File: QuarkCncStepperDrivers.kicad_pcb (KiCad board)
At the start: 4 copper layers, 35.6 x 41.9 mm, 61 parts, among them J1 Conn_01x14, J2 Conn_01x14, Q1 AO4264E, Q2 AO4264E, Q3 AO4264E, Q4 AO4264E, Q5 AO4264E, Q6 AO4264E, Q7 AO4264E, Q8 AO4264E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

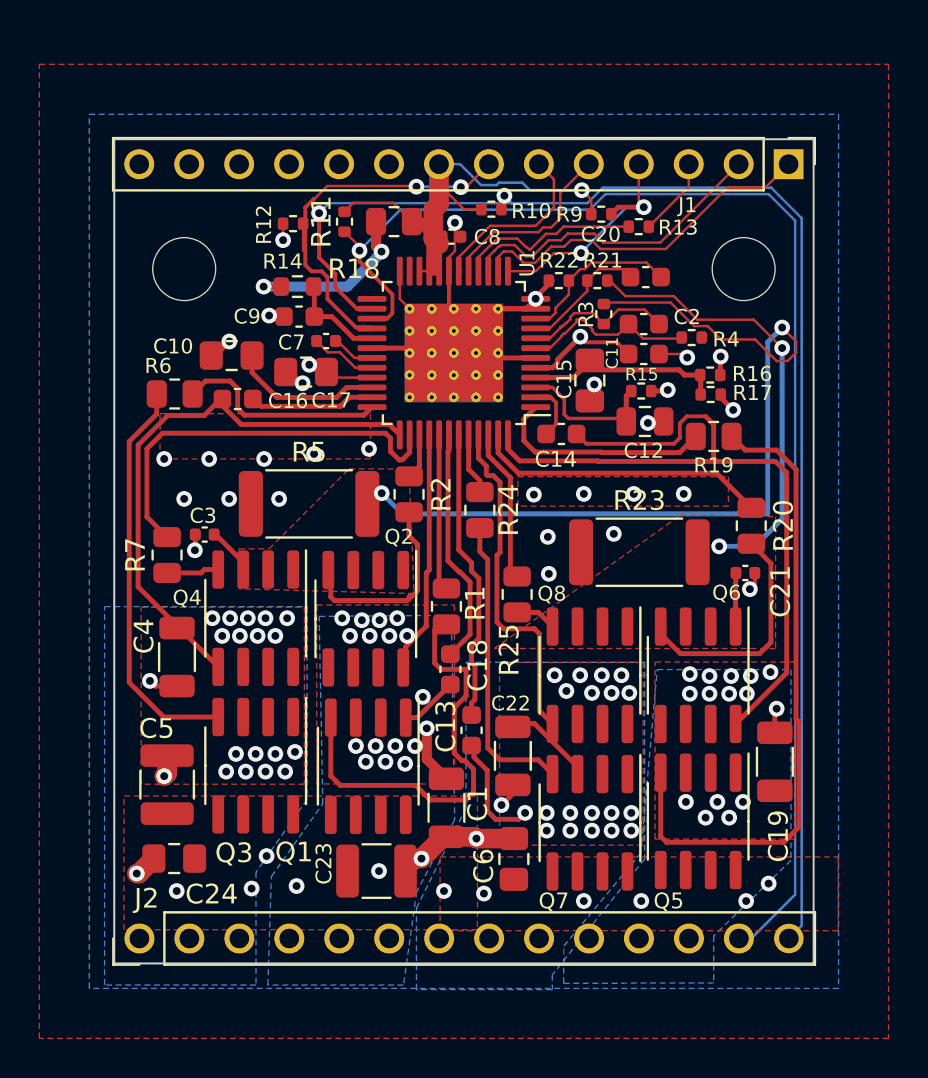
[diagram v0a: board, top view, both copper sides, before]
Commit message: Removed 0Ohms. Keyed design
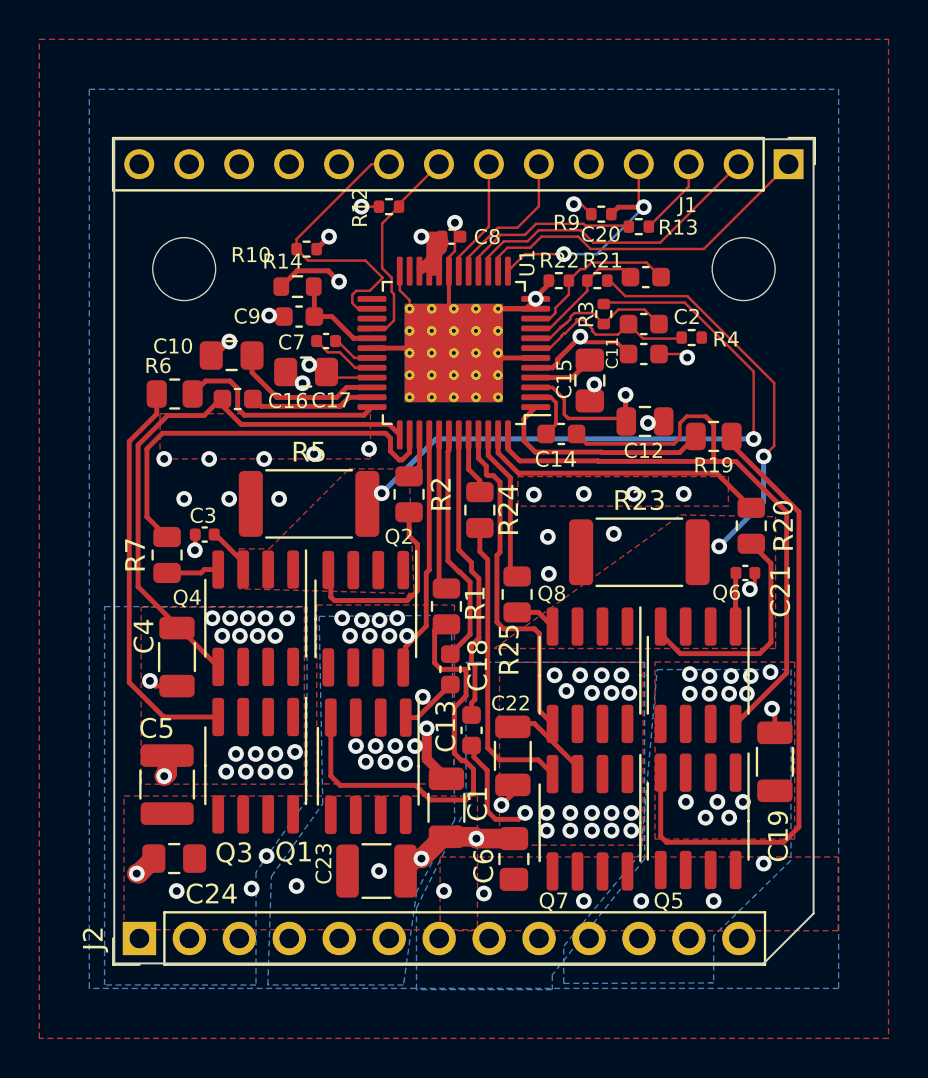
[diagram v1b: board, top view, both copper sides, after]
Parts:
- removed R11: 10k 1%, Resistor_SMD:R_0402_1005Metric
- removed R15: 0R, Resistor_SMD:R_0402_1005Metric
- removed R16, R17: 0R DNI, Resistor_SMD:R_0402_1005Metric
- removed R18: 0R DNI, Resistor_SMD:R_0805_2012Metric
- J2: value Conn_01x14 -> Conn_01x13; footprint Connector_PinHeader_2.54mm:PinHeader_1x14_P2.54mm_Vertical -> Connector_PinHeader_2.54mm:PinHeader_1x13_P2.54mm_Vertical
- moved R10 9.62 mm to (110.1, 109.1), turned to 0 degrees
- moved R12 4.95 mm to (114.3, 106.9)
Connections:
- C12 pad 1: /STEPPER DRIVER X/TMC5160_12VOUT -> +12V
- J1 pad 10: GND -> +3V3
- J1 pad 5: /STEPPER_X_STEP -> GND
- J1 pad 6: /STEPPER_X_DIR -> /STEPPER_X_STEP
- J1 pad 7: /STEPPER_X_ENn -> /STEPPER_X_DIR
- J1 pad 8: +3V3 -> /STEPPER_X_ENn
- J1 pad 9: +12V -> /STEPPER_DIAG0
- J2 pad 13: /STEPPER_DIAG1 -> +12V
- R10 pad 1: /STEPPER_DIAG2 -> /STEPPER_DIAG0
- U1 pad 26: /STEPPER_DIAG2 -> /STEPPER_DIAG0
- U1 pad 27: /STEPPER_DIAG1 -> unconnected-(U1-Pad27)
- U1 pad 3: /STEPPER DRIVER X/TMC5160_12VOUT -> +12V
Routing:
- net /STEPPER_DIAG2: track 70.9 -> 0.00 mm, vias 2 -> 0
- net /STEPPER_DIAG1: track 68.5 -> 0.00 mm, vias 1 -> 0
- net +3V3: track 26.4 -> 8.37 mm, vias 1 -> 3
- net +12V: track 25.8 -> 43.7 mm, vias 2 -> 1
- net /STEPPER_DIAG0: track 0.00 -> 15.2 mm
- net /STEPPER DRIVER X/hbridge_A3/hbridge_low_side: track 45.0 -> 34.9 mm
- net /STEPPER_X_ENn: track 20.6 -> 11.3 mm, vias 2 -> 0
- net /STEPPER DRIVER X/TMC5160_12VOUT: track 7.37 -> 0.00 mm
- net /STEPPER DRIVER X/VSA: track 9.60 -> 3.12 mm
- net /STEPPER DRIVER X/5VOUT: track 27.5 -> 23.3 mm, vias 3 -> 2
- net /STEPPER_X_DIR: track 9.12 -> 6.07 mm
- net /STEPPER DRIVER X/hbridge_A2/hbridge_low_side: track 25.4 -> 22.7 mm
- net /STEPPER_X_STEP: track 9.55 -> 7.50 mm
- net /STEPPER_COIL_B1: track 39.5 -> 38.4 mm
- net Net-(Q5-Pad4): track 32.9 -> 32.0 mm
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- added copper zone on In2.Cu, net +3V3
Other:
- outline, holes or cut-outs redrawn

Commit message: Updated pinout
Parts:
- removed J2: Conn_01x13, Connector_PinHeader_2.54mm:PinHeader_1x13_P2.54mm_Vertical
- added J3: Conn_01x14, Connector_PinHeader_2.54mm:PinHeader_1x14_P2.54mm_Vertical, F.Cu at (101.6, 144.1)
- added R8: 10k 1%, Resistor_SMD:R_0402_1005Metric, F.Cu at (111.5, 111.5)
- moved R12 1.54 mm to (115.8, 107.2)
- moved R10 0.74 mm to (109.7, 108.5)
- moved C9 0.25 mm to (109.5, 112.5)
- moved R14 0.17 mm to (109.5, 111.0)
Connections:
- J1 pad 9: /STEPPER_DIAG0 -> +12V
- U1 pad 27: unconnected-(U1-Pad27) -> /STEPPER_DIAG1
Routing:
- net /STEPPER_DIAG1: track 0.00 -> 75.8 mm, vias 0 -> 2
- net /STEPPER_DIAG0: track 15.2 -> 72.7 mm, vias 0 -> 2
- net /STEPPER_X_CSn: track 12.3 -> 19.1 mm
- net /STEPPER_MISO: track 4.02 -> 7.25 mm
- net +12V: track 43.7 -> 46.1 mm
- net +3V3: track 8.37 -> 10.3 mm
- net /STEPPER_MOSI: track 15.9 -> 17.1 mm
- net /STEPPER_X_STEP: track 7.50 -> 6.96 mm
- net /STEPPER DRIVER X/LA2: track 20.6 -> 20.1 mm
